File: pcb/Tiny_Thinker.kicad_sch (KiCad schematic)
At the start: 37 parts, among them J1 USB_B_Micro, J2 Conn_02x20_Odd_Even, J3 SWD, J4 SPI1, J5 I2C1_A, J6 I2C1_B, J7 Conn_02x20_Odd_Even, SW1 SW_Push, SW2 SW_SPDT, U1 STM32F446RET6, U2 AMS1117-3.3, Y1 16MHz

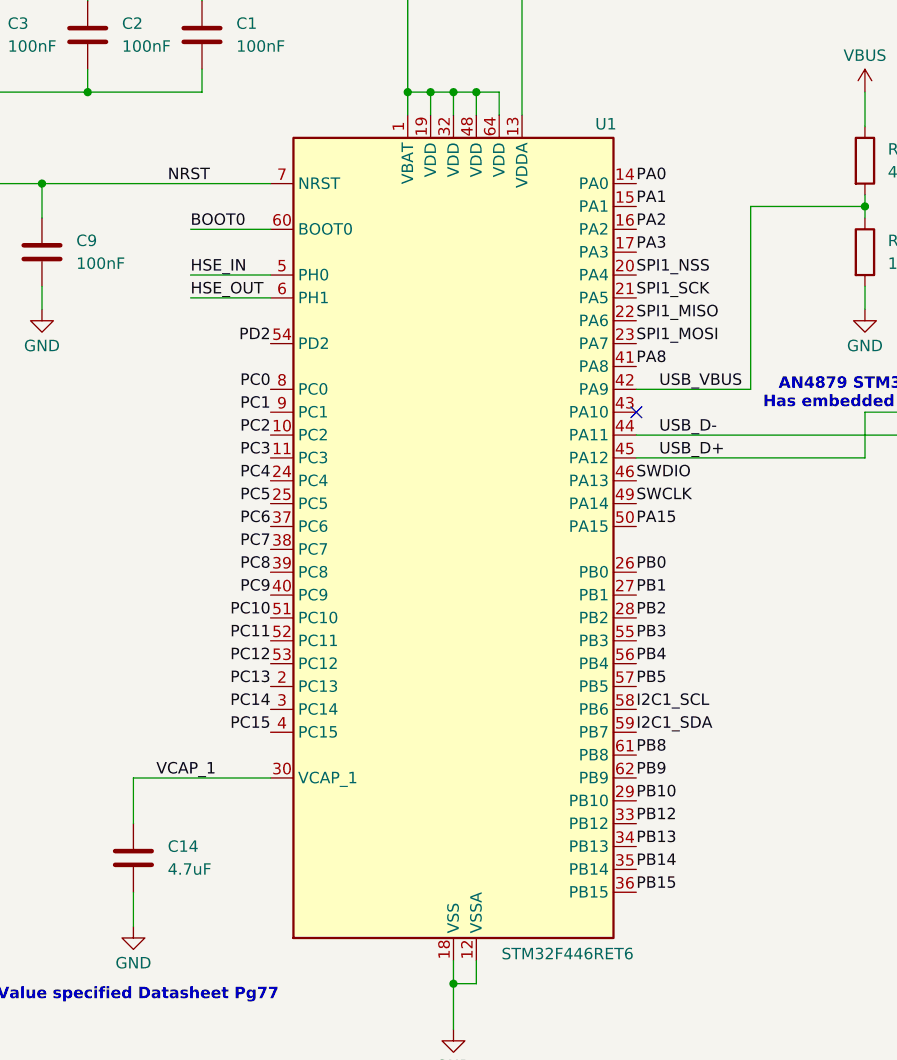
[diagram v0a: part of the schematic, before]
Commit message: changed pinout
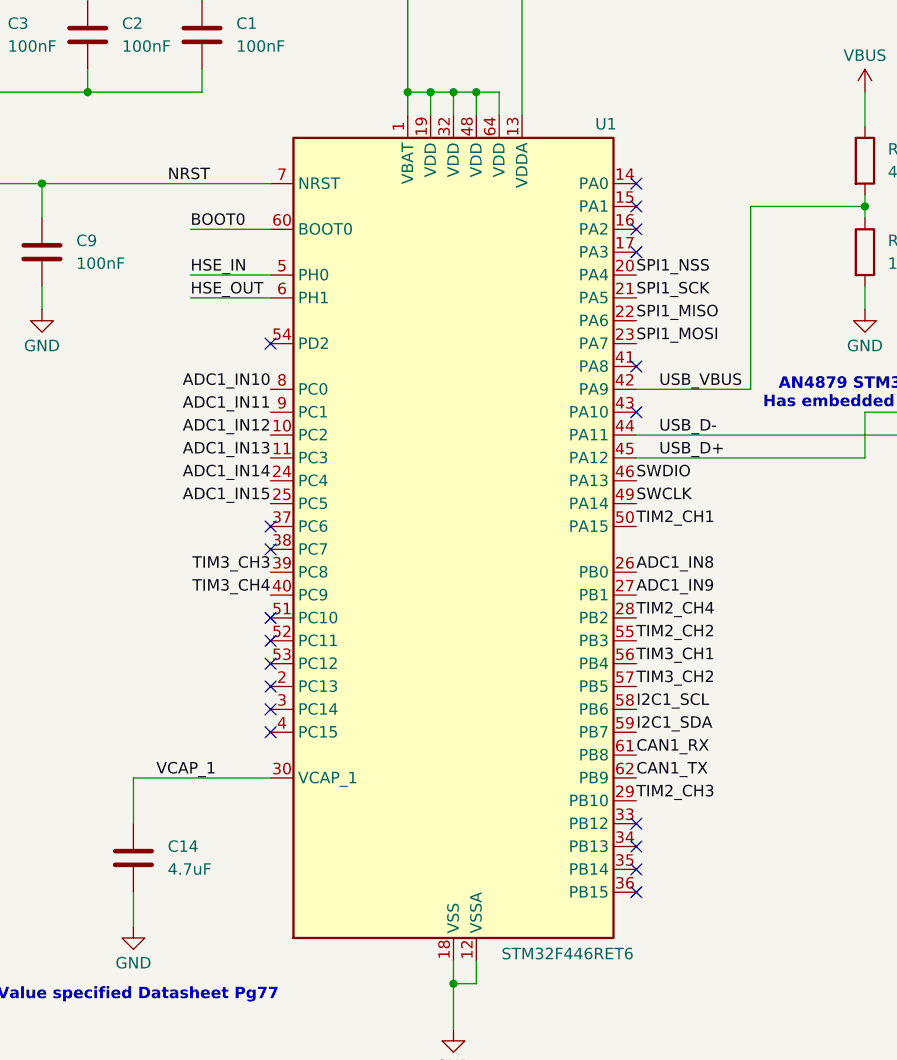
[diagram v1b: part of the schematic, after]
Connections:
- net PA0: no longer U1.14 (PA0)
- net PA1: no longer U1.15 (PA1)
- net PA15: no longer U1.50 (PA15)
- net PA2: no longer U1.16 (PA2)
- net PA3: no longer U1.17 (PA3)
- net PA8: no longer U1.41 (PA8)
- net PB0: no longer U1.26 (PB0)
- net PB1: no longer U1.27 (PB1)
- net PB10: no longer U1.29 (PB10)
- net PB12: no longer U1.33 (PB12)
- net PB13: no longer U1.34 (PB13)
- net PB14: no longer U1.35 (PB14)
- net PB15: no longer U1.36 (PB15)
- net PB2: no longer U1.28 (PB2)
- net PB3: no longer U1.55 (PB3)
- net PB4: no longer U1.56 (PB4)
- net PB5: no longer U1.57 (PB5)
- net PB8: no longer U1.61 (PB8)
- net PB9: no longer U1.62 (PB9)
- net PC0: no longer U1.8 (PC0)
- net PC1: no longer U1.9 (PC1)
- net PC10: no longer U1.51 (PC10)
- net PC11: no longer U1.52 (PC11)
- net PC12: no longer U1.53 (PC12)
- net PC13: no longer U1.2 (PC13)
- net PC14: no longer U1.3 (PC14)
- net PC15: no longer U1.4 (PC15)
- net PC2: no longer U1.10 (PC2)
- net PC3: no longer U1.11 (PC3)
- net PC4: no longer U1.24 (PC4)
- net PC5: no longer U1.25 (PC5)
- net PC6: no longer U1.37 (PC6)
- net PC7: no longer U1.38 (PC7)
- net PC8: no longer U1.39 (PC8)
- net PC9: no longer U1.40 (PC9)
- net PD2: no longer U1.54 (PD2)
- new net ADC1_IN10: U1.8 (PC0)
- new net ADC1_IN11: U1.9 (PC1)
- new net ADC1_IN12: U1.10 (PC2)
- new net ADC1_IN13: U1.11 (PC3)
- new net ADC1_IN14: U1.24 (PC4)
- new net ADC1_IN15: U1.25 (PC5)
- new net ADC1_IN8: U1.26 (PB0)
- new net ADC1_IN9: U1.27 (PB1)
- new net CAN1_RX: U1.61 (PB8)
- new net CAN1_TX: U1.62 (PB9)
- new net TIM2_CH1: U1.50 (PA15)
- new net TIM2_CH2: U1.55 (PB3)
- new net TIM2_CH3: U1.29 (PB10)
- new net TIM2_CH4: U1.28 (PB2)
- new net TIM3_CH1: U1.56 (PB4)
- new net TIM3_CH2: U1.57 (PB5)
- new net TIM3_CH3: U1.39 (PC8)
- new net TIM3_CH4: U1.40 (PC9)
- no-connect marks 4 -> 22
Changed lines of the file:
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@@
+	)
+	(no_connect
+		(at 222.25 121.92)
+	)
+	(no_connect
+		(at 181.61 162.56)
+	)
+	(no_connect
+		(at 181.61 167.64)
 	)
 	(no_connect
@@
 	)
 	(no_connect
+		(at 222.25 187.96)
+	)
+	(no_connect
+		(at 222.25 190.5)
+	)
+	(no_connect
 		(at 325.12 215.9)
+	)
+	(no_connect
+		(at 222.25 116.84)
+	)
+	(no_connect
+		(at 222.25 114.3)
+	)
+	(no_connect
+		(at 222.25 193.04)
+	)
+	(no_connect
+		(at 181.61 152.4)
+	)
+	(no_connect
+		(at 222.25 119.38)
 	)
 	(no_connect
 		(at 337.82 215.9)
 	)
+	(no_connect
+		(at 181.61 175.26)
+	)
+	(no_connect
+		(at 222.25 134.62)
+	)
+	(no_connect
+		(at 181.61 154.94)
+	)
+	(no_connect
+		(at 222.25 185.42)
+	)
+	(no_connect
+		(at 181.61 132.08)
+	)
+	(no_connect
+		(at 181.61 165.1)
+	)
+	(no_connect
+		(at 181.61 170.18)
+	)
+	(no_connect
+		(at 181.61 172.72)
+	)
 	(wire
 		(pts
@@
 		)
 	)
-	(label "PC13"
-		(at 181.61 170.18 180)
-		(effects
-			(font
-				(size 1.27 1.27)
-			)
-			(justify right bottom)
-		)
-	)
-	(label "PB4"
+	(label "TIM3_CH1"
 		(at 222.25 167.64 0)
 		(effects
@@
 		)
 	)
-	(label "PB5"
+	(label "TIM3_CH2"
 		(at 222.25 170.18 0)
-		(effects
-			(font
-				(size 1.27 1.27)
-			)
-			(justify left bottom)
-		)
-	)
-	(label "PA2"
-		(at 222.25 119.38 0)
 		(effects
 			(font
@@
 		)
 	)
-	(label "PC4"
+	(label "ADC1_IN14"
 		(at 181.61 147.32 180)
 		(effects
@@
 		)
 	)
-	(label "PB13"
-		(at 222.25 187.96 0)
-		(effects
-			(font
-				(size 1.27 1.27)
-			)
-			(justify left bottom)
-		)
-	)
 	(label "SPI1_MOSI"
 		(at 222.25 132.08 0)
@@
 		)
 	)
-	(label "PC9"
+	(label "TIM3_CH4"
 		(at 181.61 160.02 180)
 		(effects
@@
 			)
 			(justify right bottom)
-		)
-	)
-	(label "PB15"
-		(at 222.25 193.04 0)
-		(effects
-			(font
-				(size 1.27 1.27)
-			)
-			(justify left bottom)
 		)
 	)
@@
 		)
 	)
-	(label "PA8"
-		(at 222.25 134.62 0)
-		(effects
-			(font
-				(size 1.27 1.27)
-			)
-			(justify left bottom)
-		)
-	)
 	(label "PB0"
 		(at 326.39 132.08 180)
@@
 		)
 	)
-	(label "PB10"
+	(label "TIM2_CH3"
 		(at 222.25 182.88 0)
 		(effects
@@
 		)
 	)
-	(label "PC0"
+	(label "ADC1_IN10"
 		(at 181.61 137.16 180)
 		(effects
@@
 		)
 	)
-	(label "PB2"
+	(label "TIM2_CH4"
 		(at 222.25 162.56 0)
 		(effects
@@
 		)
 	)
-	(label "PC10"
-		(at 181.61 162.56 180)
-		(effects
-			(font
-				(size 1.27 1.27)
-			)
-			(justify right bottom)
-		)
-	)
-	(label "PC12"
-		(at 181.61 167.64 180)
-		(effects
-			(font
-				(size 1.27 1.27)
-			)
-			(justify right bottom)
-		)
-	)
-	(label "PA15"
+	(label "TIM2_CH1"
 		(at 222.25 152.4 0)
 		(effects
@@
 		)
 	)
-	(label "PC8"
+	(label "TIM3_CH3"
 		(at 181.61 157.48 180)
 		(effects
@@
 		)
 	)
-	(label "PB3"
+	(label "TIM2_CH2"
 		(at 222.25 165.1 0)
-		(effects
-			(font
-				(size 1.27 1.27)
-			)
-			(justify left bottom)
-		)
-	)
-	(label "PA1"
-		(at 222.25 116.84 0)
 		(effects
 			(font
@@
 		)
 	)
-	(label "PB14"
-		(at 222.25 190.5 0)
-		(effects
-			(font
-				(size 1.27 1.27)
-			)
-			(justify left bottom)
-		)
-	)
 	(label "PD2"
 		(at 337.82 182.88 0)
@@
 		)
 	)
-	(label "PC15"
-		(at 181.61 175.26 180)
-		(effects
-			(font
-				(size 1.27 1.27)
-			)
-			(justify right bottom)
-		)
-	)
 	(label "NRST"
 		(at 170.18 114.3 0)
@@
 		)
 	)
-	(label "PC14"
-		(at 181.61 172.72 180)
-		(effects
-			(font
-				(size 1.27 1.27)
-			)
-			(justify right bottom)
-		)
-	)
-	(label "PC1"
+	(label "ADC1_IN11"
 		(at 181.61 139.7 180)
 		(effects
@@
 		)
 	)
-	(label "PC5"
+	(label "ADC1_IN15"
 		(at 181.61 149.86 180)
 		(effects
@@
 		)
 	)
-	(label "PB8"
+	(label "CAN1_RX"
 		(at 222.25 177.8 0)
 		(effects
@@
 		)
 	)
-	(label "PB0"
+	(label "ADC1_IN8"
 		(at 222.25 157.48 0)
 		(effects
@@
 		)
 	)
-	(label "PB9"
+	(label "CAN1_TX"
 		(at 222.25 180.34 0)
 		(effects
@@
 		)
 	)
-	(label "PC7"
-		(at 181.61 154.94 180)
-		(effects
-			(font
-				(size 1.27 1.27)
-			)
-			(justify right bottom)
-		)
-	)
 	(label "I2C1_SDA"
 		(at 298.45 196.85 180)
@@
 		)
 	)
-	(label "PA3"
-		(at 222.25 121.92 0)
-		(effects
-			(font
-				(size 1.27 1.27)
-			)
-			(justify left bottom)
-		)
-	)
-	(label "PB12"
-		(at 222.25 185.42 0)
-		(effects
-			(font
-				(size 1.27 1.27)
-			)
-			(justify left bottom)
-		)
-	)
 	(label "I2C1_SCL"
 		(at 222.25 172.72 0)
@@
 		)
 	)
-	(label "PB1"
+	(label "ADC1_IN9"
 		(at 222.25 160.02 0)
 		(effects
@@
 		)
 	)
-	(label "PA0"
-		(at 222.25 114.3 0)
-		(effects
-			(font
-				(size 1.27 1.27)
-			)
-			(justify left bottom)
-		)
-	)
-	(label "PD2"
-		(at 181.61 132.08 180)
-		(effects
-			(font
-				(size 1.27 1.27)
-			)
-			(justify right bottom)
-		)
-	)
-	(label "PC11"
-		(at 181.61 165.1 180)
-		(effects
-			(font
-				(size 1.27 1.27)
-			)
-			(justify right bottom)
-		)
-	)
 	(label "PWR_LED_K"
 		(at 342.9 43.18 0)
@@
 		)
 	)
-	(label "PC2"
+	(label "ADC1_IN12"
 		(at 181.61 142.24 180)
 		(effects
@@
 		)
 	)
-	(label "PC3"
+	(label "ADC1_IN13"
 		(at 181.61 144.78 180)
 		(effects
 			(font
-				(size 1.27 1.27)
-			)
-			(justify right bottom)
-		)
-	)
-	(label "PC6"
-		(at 181.61 152.4 180)
-		(effects
-			(font

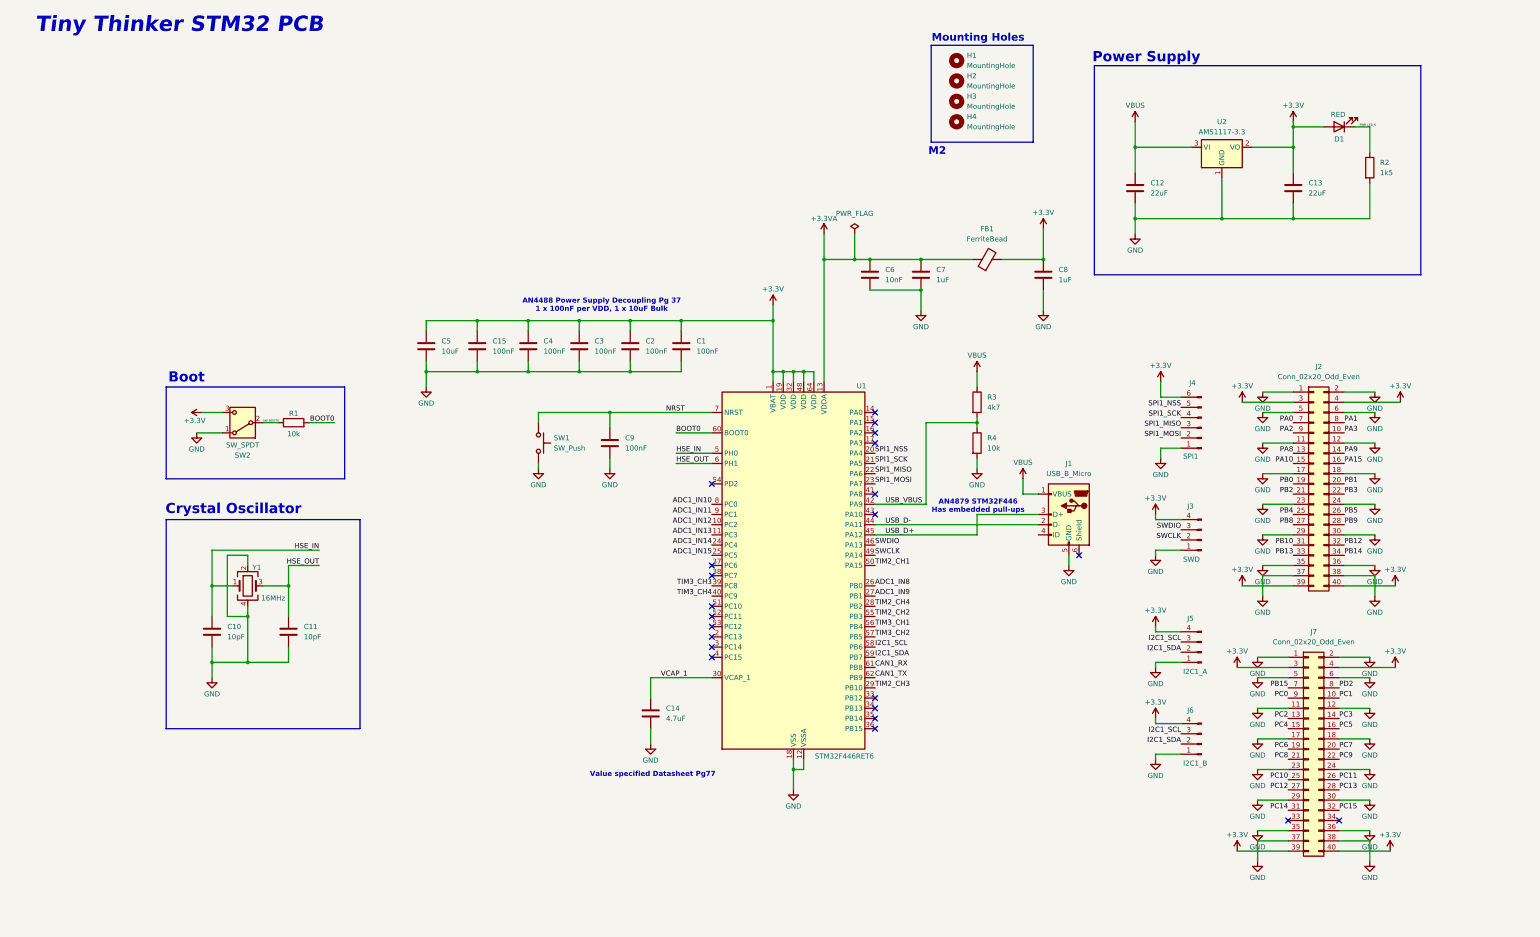
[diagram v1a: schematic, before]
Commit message: added more comments are made the schematic neater
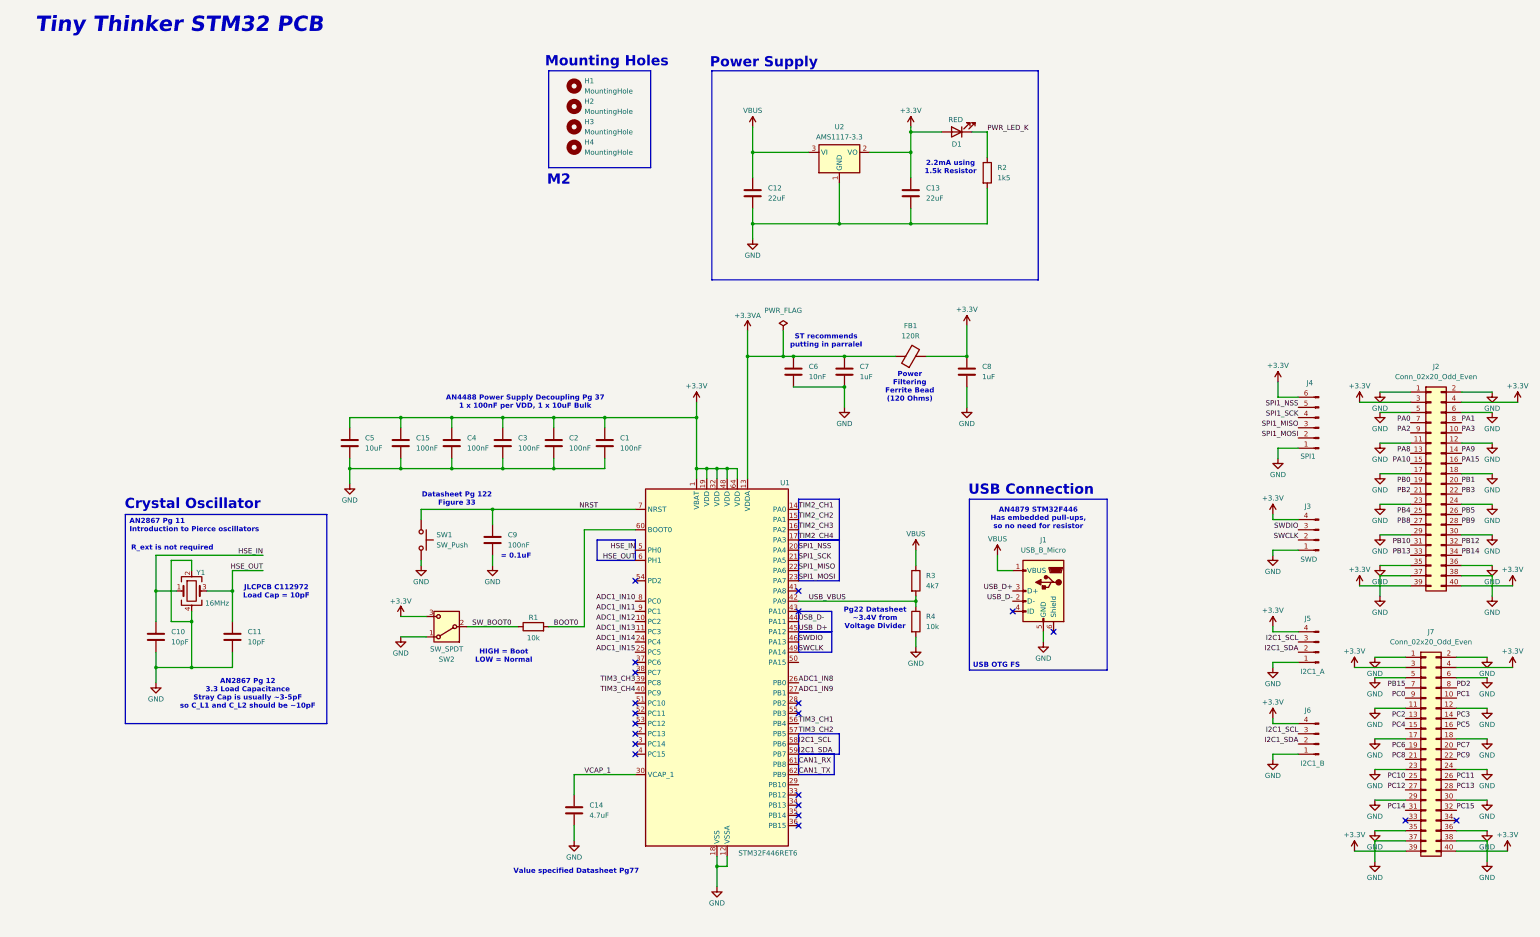
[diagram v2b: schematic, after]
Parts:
- FB1: value FerriteBead -> 120R
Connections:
- net TIM2_CH1: now also U1.14 (PA0); no longer U1.50 (PA15)
- net TIM2_CH2: now also U1.15 (PA1); no longer U1.55 (PB3)
- net TIM2_CH3: now also U1.16 (PA2); no longer U1.29 (PB10)
- net TIM2_CH4: now also U1.17 (PA3); no longer U1.28 (PB2)
- no-connect marks 22 -> 21
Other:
- note added: "2.2mA using 1.5k Resistor"
- note added: "= 0.1uF"
- note added: "AN2867 Pg 11 Introduction to Pierce oscillators"
- note added: "AN2867 Pg 12 3.3 Load Capacitance Stray Cap is usually ~3-5pF so C_L1 and C_L2 should be ~10pF"
- note added: "AN4879 STM32F446 Has embedded pull-ups, so no need for resistor"
- note added: "Datasheet Pg 122 Figure 33"
- note added: "HIGH = Boot LOW = Normal"
- note added: "JLCPCB C112972 Load Cap = 10pF"
- note added: "Pg22 Datasheet ~3.4V from Voltage Divider"
- note added: "Power Filtering Ferrite Bead (120 Ohms)"
- note added: "R_ext is not required"
- note added: "ST recommends putting in parralel"
- note added: "USB Connection"
- note added: "USB OTG FS"
- note removed: "AN4879 STM32F446 Has embedded pull-ups"
- note removed: "Boot"
- moved on the sheet: C1, C10, C11, C12, C13, C14, C15, C2, C3, C4, C5, C6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

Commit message: added USB C with ESD Protection
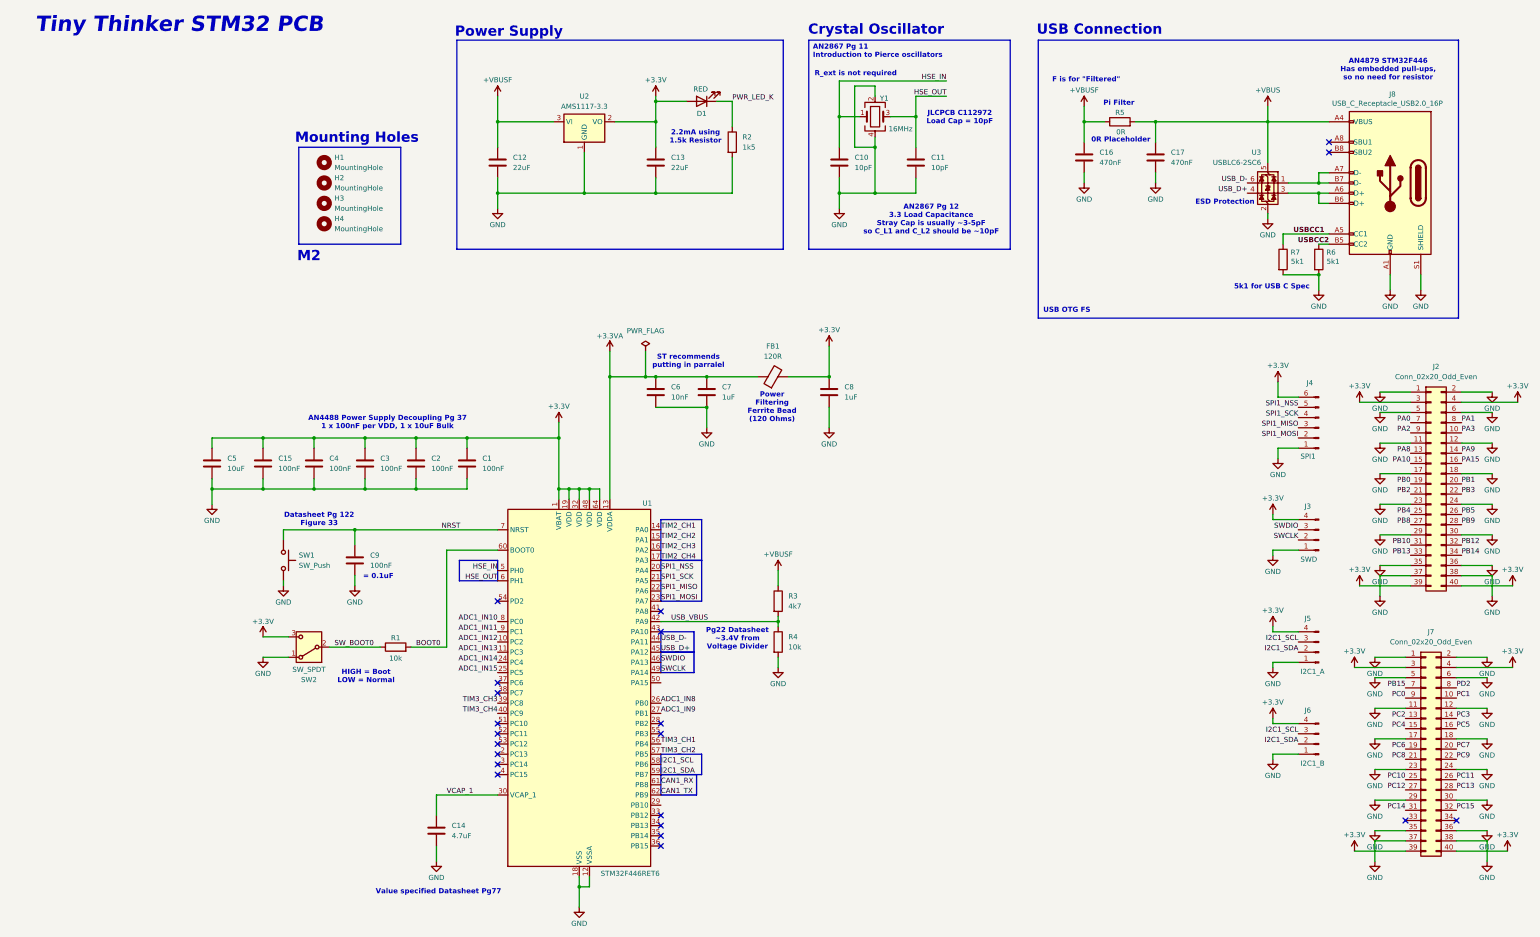
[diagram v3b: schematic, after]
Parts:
- removed J1: USB_B_Micro, Connector_USB:USB_Micro-B_Amphenol_10118194_Horizontal, symbol Connector:USB_B_Micro
- added C16, C17: 470nF, symbol Device:C
- added J8: USB_C_Receptacle_USB2.0_16P, Connector_USB:USB_C_Receptacle_GCT_USB4105-xx-A_16P_TopMnt_Horizontal, symbol Connector:USB_C_Receptacle_USB2.0_16P
- added R5: 0R, symbol Device:R
- added R6, R7: 5k1, symbol Device:R
- added U3: USBLC6-2SC6, Package_TO_SOT_SMD:SOT-23-6, symbol Power_Protection:USBLC6-2SC6
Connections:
- net GND: now also C16.2, C17.2, J8.A1 (GND), J8.A12 (GND), J8.B1 (GND), J8.B12 (GND), J8.S1 (SHIELD), R6.2, R7.2, U3.2 (GND)
- net USB_D+: now also U3.4 (I/O2)
- net USB_D-: now also U3.6 (I/O1)
- net VBUS renamed +VBUSF
- net +VBUSF: now also C16.1, R5.1
- new net: J8.A6 (D+), J8.B6 (D+), U3.3 (I/O2)
- new net: J8.A7 (D-), J8.B7 (D-), U3.1 (I/O1)
- new net +VBUS: C17.1, J8.A4 (VBUS), J8.A9 (VBUS), J8.B4 (VBUS), J8.B9 (VBUS), R5.2, U3.5 (VBUS)
- new net USBCC1: J8.A5 (CC1), R7.1
- new net USBCC2: J8.B5 (CC2), R6.1
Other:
- note added: "0R Placeholder"
- note added: "5k1 for USB C Spec"
- note added: "ESD Protection"
- note added: "F is for "Filtered""
- note added: "Pi Filter"
- moved on the sheet: C1, C10, C11, C12, C13, C14, C15, C2, C3, C4, C5, C6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
